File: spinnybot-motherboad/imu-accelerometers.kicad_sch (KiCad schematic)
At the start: 17 parts, among them U4 ICM-20649

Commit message: PCB schematic (hopefully) finished
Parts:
- added R? (x2): 10k, symbol Device:R
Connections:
- net ACCEL_SELF_TEST: now also R?.1, R?.1
- net GND: now also R?.2, R?.2

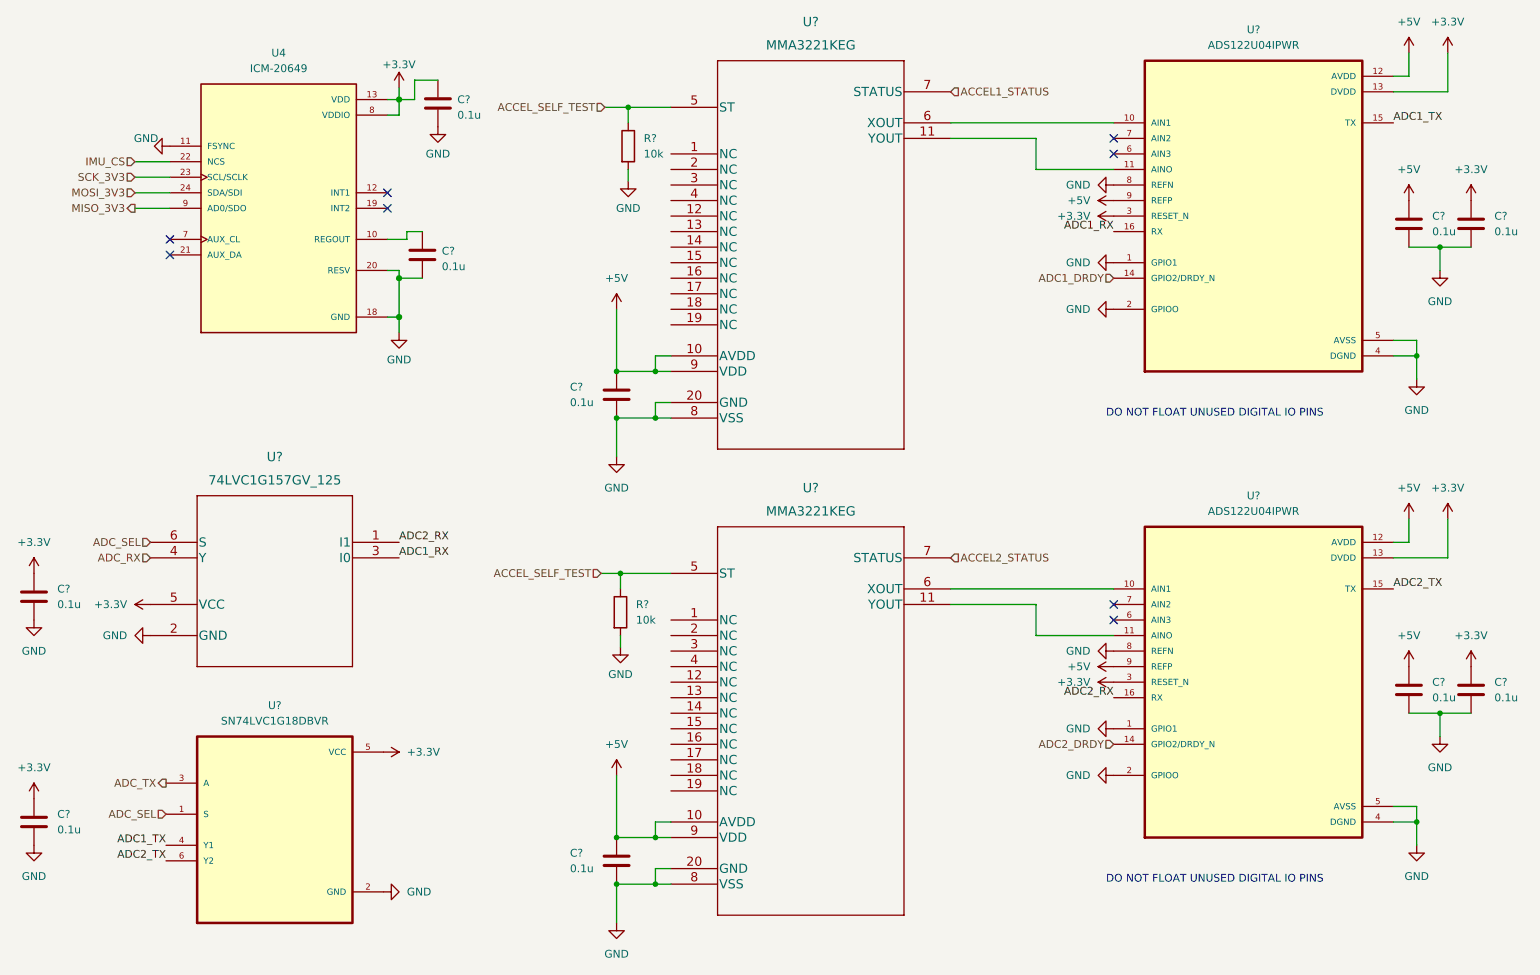
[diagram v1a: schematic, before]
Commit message: Added 4 pin JST connector footprint and assigned footprints
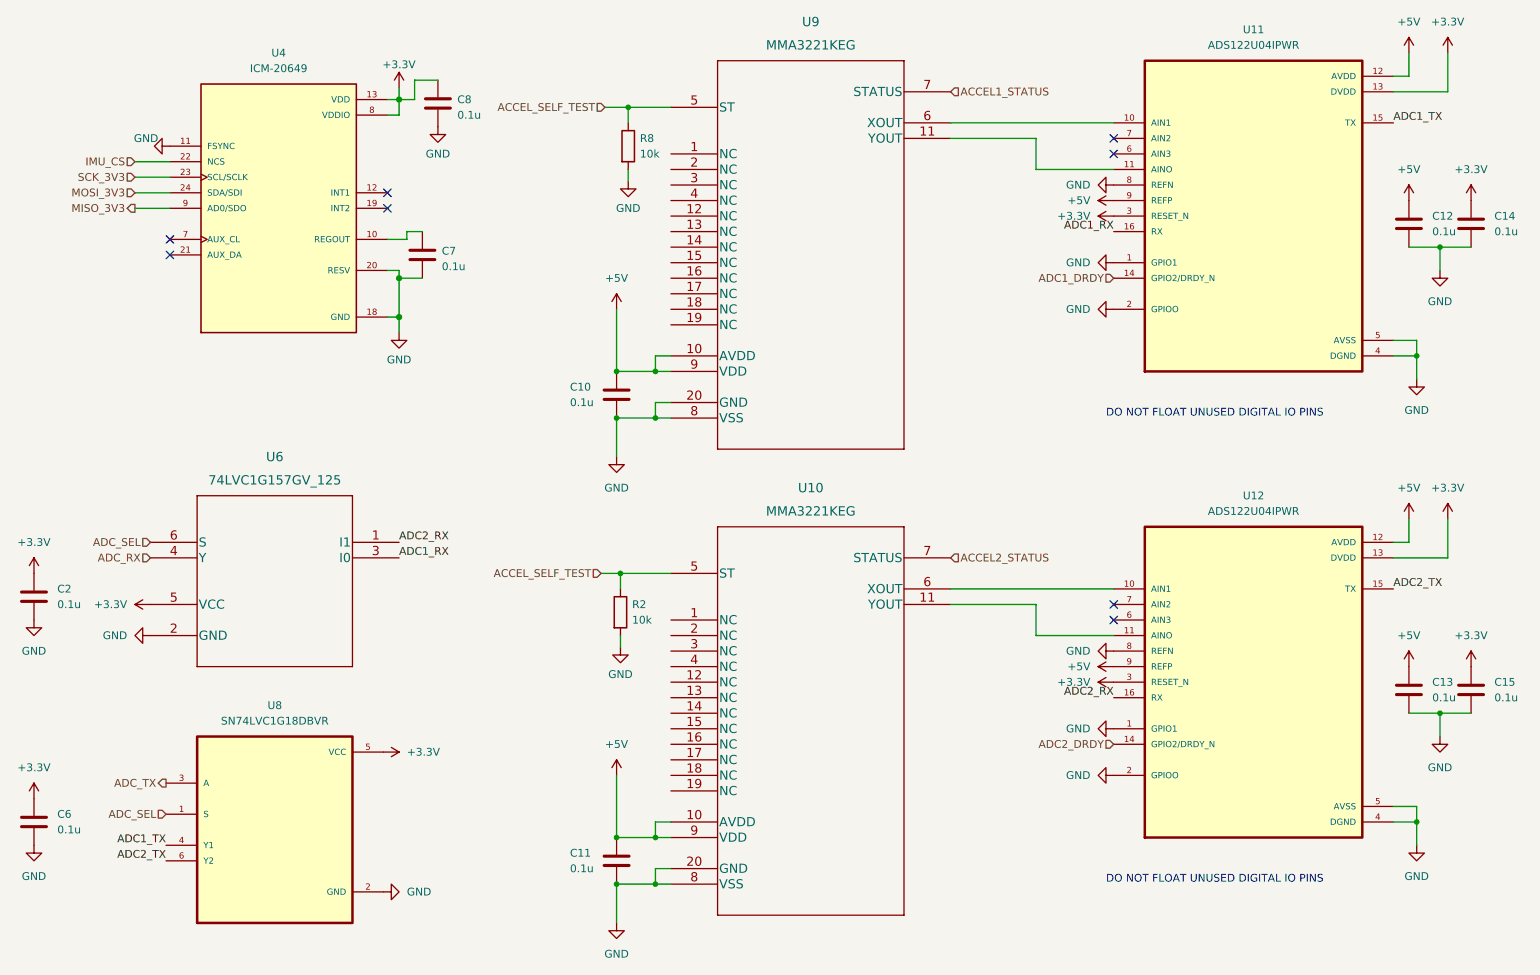
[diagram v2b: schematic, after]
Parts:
- C10, C11, C12, C13, C14, C15, C2, C6: renamed from C?; footprint (none) -> Capacitor_SMD:C_0805_2012Metric_Pad1.18x1.45mm_HandSolder
- R2, R8: renamed from R?; footprint (none) -> Resistor_SMD:R_0805_2012Metric_Pad1.20x1.40mm_HandSolder
- gave numbers to parts that had none: 8
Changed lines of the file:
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@@
   (symbol (lib_id "Device:C") (at 87.63 33.655 0) (unit 1)
     (in_bom yes) (on_board yes) (fields_autoplaced)
-    (property "Reference" "C?" (id 0) (at 90.805 33.0199 0)
+    (property "Reference" "C8" (id 0) (at 90.805 33.0199 0)
       (effects (font (size 1.27 1.27)) (justify left))
     )
@@
   (symbol (lib_id "MMA3221KEG:MMA3221KEG") (at 125.73 110.49 0) (unit 1)
     (in_bom yes) (on_board yes) (fields_autoplaced)
-    (property "Reference" "U?" (id 0) (at 148.59 96.52 0)
+    (property "Reference" "U10" (id 0) (at 148.59 96.52 0)
       (effects (font (size 1.524 1.524)))
     )
@@
   (symbol (lib_id "Device:C") (at 256.54 129.54 0) (unit 1)
     (in_bom yes) (on_board yes) (fields_autoplaced)
-    (property "Reference" "C?" (id 0) (at 260.35 128.2699 0)
+    (property "Reference" "C15" (id 0) (at 260.35 128.2699 0)
       (effects (font (size 1.27 1.27)) (justify left))
     )
@@
       (effects (font (size 1.27 1.27)) (justify left))
     )
-    (property "Footprint" "" (id 2) (at 257.5052 133.35 0)
+    (property "Footprint" "Capacitor_SMD:C_0805_2012Metric_Pad1.18x1.45mm_HandSolder" (id 2) (at 257.5052 133.35 0)
       (effects (font (size 1.27 1.27)) hide)
     )
@@
   (symbol (lib_id "Device:C") (at 21.59 151.13 0) (unit 1)
     (in_bom yes) (on_board yes) (fields_autoplaced)
-    (property "Reference" "C?" (id 0) (at 25.4 149.8599 0)
+    (property "Reference" "C6" (id 0) (at 25.4 149.8599 0)
       (effects (font (size 1.27 1.27)) (justify left))
     )
@@
       (effects (font (size 1.27 1.27)) (justify left))
     )
-    (property "Footprint" "" (id 2) (at 22.5552 154.94 0)
+    (property "Footprint" "Capacitor_SMD:C_0805_2012Metric_Pad1.18x1.45mm_HandSolder" (id 2) (at 22.5552 154.94 0)
       (effects (font (size 1.27 1.27)) hide)
     )
@@
   (symbol (lib_id "Device:C") (at 246.38 129.54 0) (unit 1)
     (in_bom yes) (on_board yes) (fields_autoplaced)
-    (property "Reference" "C?" (id 0) (at 250.19 128.2699 0)
+    (property "Reference" "C13" (id 0) (at 250.19 128.2699 0)
       (effects (font (size 1.27 1.27)) (justify left))
     )
@@
       (effects (font (size 1.27 1.27)) (justify left))
     )
-    (property "Footprint" "" (id 2) (at 247.3452 133.35 0)
+    (property "Footprint" "Capacitor_SMD:C_0805_2012Metric_Pad1.18x1.45mm_HandSolder" (id 2) (at 247.3452 133.35 0)
       (effects (font (size 1.27 1.27)) hide)
     )
@@
   (symbol (lib_id "Device:C") (at 21.59 114.3 0) (unit 1)
     (in_bom yes) (on_board yes) (fields_autoplaced)
-    (property "Reference" "C?" (id 0) (at 25.4 113.0299 0)
+    (property "Reference" "C2" (id 0) (at 25.4 113.0299 0)
       (effects (font (size 1.27 1.27)) (justify left))
     )
@@
       (effects (font (size 1.27 1.27)) (justify left))
     )
-    (property "Footprint" "" (id 2) (at 22.5552 118.11 0)
+    (property "Footprint" "Capacitor_SMD:C_0805_2012Metric_Pad1.18x1.45mm_HandSolder" (id 2) (at 22.5552 118.11 0)
       (effects (font (size 1.27 1.27)) hide)
     )
@@
   (symbol (lib_id "Device:C") (at 85.09 58.42 0) (unit 1)
     (in_bom yes) (on_board yes) (fields_autoplaced)
-    (property "Reference" "C?" (id 0) (at 88.265 57.7849 0)
+    (property "Reference" "C7" (id 0) (at 88.265 57.7849 0)
       (effects (font (size 1.27 1.27)) (justify left))
     )
@@
   (symbol (lib_id "Device:R") (at 118.745 40.64 0) (unit 1)
     (in_bom yes) (on_board yes) (fields_autoplaced)
-    (property "Reference" "R?" (id 0) (at 121.285 39.3699 0)
-      (effects (font (size 1.27 1.27)) (justify left))
-    )
-    (property "Value" "10k" (id 1) (at 121.285 41.9099 0)
-      (effects (font (size 1.27 1.27)) (justify left))
-    )
-    (property "Footprint" "" (id 2) (at 116.967 40.64 90)
+    (property "Reference" "R8" (id 0) (at 120.65 39.3699 0)
+      (effects (font (size 1.27 1.27)) (justify left))
+    )
+    (property "Value" "10k" (id 1) (at 120.65 41.9099 0)
+      (effects (font (size 1.27 1.27)) (justify left))
+    )
+    (property "Footprint" "Resistor_SMD:R_0805_2012Metric_Pad1.20x1.40mm_HandSolder" (id 2) (at 116.967 40.64 90)
       (effects (font (size 1.27 1.27)) hide)
     )
@@
   (symbol (lib_id "Device:C") (at 116.84 157.48 0) (unit 1)
     (in_bom yes) (on_board yes)
-    (property "Reference" "C?" (id 0) (at 109.22 156.21 0)
+    (property "Reference" "C11" (id 0) (at 109.22 156.21 0)
       (effects (font (size 1.27 1.27)) (justify left))
     )
@@
       (effects (font (size 1.27 1.27)) (justify left))
     )
-    (property "Footprint" "" (id 2) (at 117.8052 161.29 0)
+    (property "Footprint" "Capacitor_SMD:C_0805_2012Metric_Pad1.18x1.45mm_HandSolder" (id 2) (at 117.8052 161.29 0)
       (effects (font (size 1.27 1.27)) hide)
     )
@@
   (symbol (lib_id "Device:R") (at 117.475 116.84 0) (unit 1)
     (in_bom yes) (on_board yes) (fields_autoplaced)
-    (property "Reference" "R?" (id 0) (at 120.015 115.5699 0)
-      (effects (font (size 1.27 1.27)) (justify left))
-    )
-    (property "Value" "10k" (id 1) (at 120.015 118.1099 0)
-      (effects (font (size 1.27 1.27)) (justify left))
-    )
-    (property "Footprint" "" (id 2) (at 115.697 116.84 90)
+    (property "Reference" "R2" (id 0) (at 119.38 115.5699 0)
+      (effects (font (size 1.27 1.27)) (justify left))
+    )
+    (property "Value" "10k" (id 1) (at 119.38 118.1099 0)
+      (effects (font (size 1.27 1.27)) (justify left))
+    )
+    (property "Footprint" "Resistor_SMD:R_0805_2012Metric_Pad1.20x1.40mm_HandSolder" (id 2) (at 115.697 116.84 90)
       (effects (font (size 1.27 1.27)) hide)
     )
@@
   (symbol (lib_id "MMA3221KEG:MMA3221KEG") (at 125.73 34.29 0) (unit 1)
     (in_bom yes) (on_board yes) (fields_autoplaced)
-    (property "Reference" "U?" (id 0) (at 148.59 20.32 0)
+    (property "Reference" "U9" (id 0) (at 148.59 20.32 0)
       (effects (font (size 1.524 1.524)))
     )
@@
   (symbol (lib_id "SN74LVC1G18DBVR:SN74LVC1G18DBVR") (at 60.96 152.4 0) (unit 1)
     (in_bom yes) (on_board yes) (fields_autoplaced)
-    (property "Reference" "U?" (id 0) (at 60.96 132.08 0))
+    (property "Reference" "U8" (id 0) (at 60.96 132.08 0))
     (property "Value" "SN74LVC1G18DBVR" (id 1) (at 60.96 134.62 0))
     (property "Footprint" "SN74LVC1G18DBVR:SOT95P280X145-6N" (id 2) (at 60.96 152.4 0)
@@
   (symbol (lib_id "Device:C") (at 246.38 53.34 0) (unit 1)
     (in_bom yes) (on_board yes) (fields_autoplaced)
-    (property "Reference" "C?" (id 0) (at 250.19 52.0699 0)
+    (property "Reference" "C12" (id 0) (at 250.19 52.0699 0)
       (effects (font (size 1.27 1.27)) (justify left))
     )
@@
       (effects (font (size 1.27 1.27)) (justify left))
     )
-    (property "Footprint" "" (id 2) (at 247.3452 57.15 0)
+    (property "Footprint" "Capacitor_SMD:C_0805_2012Metric_Pad1.18x1.45mm_HandSolder" (id 2) (at 247.3452 57.15 0)
       (effects (font (size 1.27 1.27)) hide)
     )
@@
   (symbol (lib_id "ADS122U04IPWR:ADS122U04IPWR") (at 220.98 52.07 0) (unit 1)
     (in_bom yes) (on_board yes) (fields_autoplaced)
-    (property "Reference" "U?" (id 0) (at 220.98 21.59 0))
+    (property "Reference" "U11" (id 0) (at 220.98 21.59 0))
     (property "Value" "ADS122U04IPWR" (id 1) (at 220.98 24.13 0))
     (property "Footprint" "ADS122U04IPWR:SOP65P640X120-16N" (id 2) (at 220.98 52.07 0)
@@
   (symbol (lib_id "Device:C") (at 256.54 53.34 0) (unit 1)
     (in_bom yes) (on_board yes) (fields_autoplaced)
-    (property "Reference" "C?" (id 0) (at 260.35 52.0699 0)
+    (property "Reference" "C14" (id 0) (at 260.35 52.0699 0)
       (effects (font (size 1.27 1.27)) (justify left))
     )
@@
       (effects (font (size 1.27 1.27)) (justify left))
     )
-    (property "Footprint" "" (id 2) (at 257.5052 57.15 0)
+    (property "Footprint" "Capacitor_SMD:C_0805_2012Metric_Pad1.18x1.45mm_HandSolder" (id 2) (at 257.5052 57.15 0)
       (effects (font (size 1.27 1.27)) hide)
     )
@@
   (symbol (lib_id "74LVC1G157GV,125:74LVC1G157GV_125") (at 40.64 105.41 0) (unit 1)
     (in_bom yes) (on_board yes) (fields_autoplaced)
-    (property "Reference" "U?" (id 0) (at 60.96 91.44 0)
+    (property "Reference" "U6" (id 0) (at 60.96 91.44 0)
       (effects (font (size 1.524 1.524)))
     )
@@
   (symbol (lib_id "ADS122U04IPWR:ADS122U04IPWR") (at 220.98 128.27 0) (unit 1)
     (in_bom yes) (on_board yes) (fields_autoplaced)
-    (property "Reference" "U?" (id 0) (at 220.98 97.79 0))
+    (property "Reference" "U12" (id 0) (at 220.98 97.79 0))
     (property "Value" "ADS122U04IPWR" (id 1) (at 220.98 100.33 0))
     (property "Footprint" "ADS122U04IPWR:SOP65P640X120-16N" (id 2) (at 220.98 128.27 0)
@@
   (symbol (lib_id "power:GND") (at 117.475 122.555 0) (unit 1)
     (in_bom yes) (on_board yes) (fields_autoplaced)
-    (property "Reference" "#PWR?" (id 0) (at 117.475 128.905 0)
+    (property "Reference" "#PWR0157" (id 0) (at 117.475 128.905 0)
       (effects (font (size 1.27 1.27)) hide)
     )
@@
   (symbol (lib_id "Device:C") (at 116.84 81.28 0) (unit 1)
     (in_bom yes) (on_board yes)
-    (property "Reference" "C?" (id 0) (at 109.22 80.01 0)
+    (property "Reference" "C10" (id 0) (at 109.22 80.01 0)
       (effects (font (size 1.27 1.27)) (justify left))
     )
@@
       (effects (font (size 1.27 1.27)) (justify left))
     )
-    (property "Footprint" "" (id 2) (at 117.8052 85.09 0)
-      (effects (font (size 1.27 1.27)) hide)
-    )
+    (property "Footprint" "Capacitor_SMD:C_0805_2012Metric_Pad1.18x1.45mm_HandSolder" (id 2) (at 117.8052 85.09 0)
+      (effects (font (size 1.27 1.27)) hide)
+    )
